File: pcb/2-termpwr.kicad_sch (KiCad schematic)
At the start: 0 parts

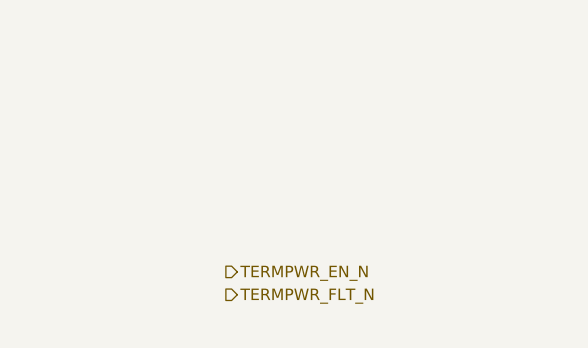
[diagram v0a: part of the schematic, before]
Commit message: Phase 3: populate power sheet; descriptive net names
Power sheet: bench eFuse (TPS259470A) with UVLO/OVLO string and EN
clamp, TPS2116 bench-priority mux with VBUS snubber, 3.3 V and 2.83 V
TPS73701 LDOs. Notes on the string's tap voltages, eFuse setting pins
and every DNP part. Project symbol library with the TPS259470A and
TPS73701DCQ drawn from the datasheet pin tables.

Nets renamed to spelled-out names (IS_BENCH_POWERED, *_INVERTED for
active-low, FEEDBACK, VTERMINATOR, TERMINATOR_EN) across the schematic,
pinout page, parts list and power block page.

Co-Authored-By: Claude Opus 5.5 <noreply@anthropic.com>
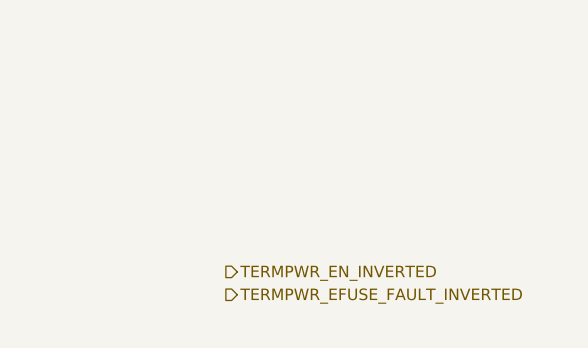
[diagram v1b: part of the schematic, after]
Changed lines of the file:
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@@
 	(hierarchical_label "CC1" (shape input) (at 50.8 53.34 180) (effects (font (size 1.27 1.27)) (justify right)))
 	(hierarchical_label "CC2" (shape input) (at 50.8 55.88 180) (effects (font (size 1.27 1.27)) (justify right)))
-	(hierarchical_label "TERMPWR_EN_N" (shape output) (at 343.8 50.8 0) (effects (font (size 1.27 1.27)) (justify left)))
-	(hierarchical_label "TERMPWR_FLT_N" (shape output) (at 343.8 53.34 0) (effects (font (size 1.27 1.27)) (justify left)))
+	(hierarchical_label "TERMPWR_EN_INVERTED" (shape output) (at 343.8 50.8 0) (effects (font (size 1.27 1.27)) (justify left)))
+	(hierarchical_label "TERMPWR_EFUSE_FAULT_INVERTED" (shape output) (at 343.8 53.34 0) (effects (font (size 1.27 1.27)) (justify left)))
 	(embedded_fonts no)
 )
